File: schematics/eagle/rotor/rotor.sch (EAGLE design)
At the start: 55 parts, among them IC1 TXS0108, IC2 7815TV, J1 PL9823, J10 TB004-508-02BE, J2 pwr2, J3 Power, J4 Antenna, J5 Power, J6 CCW, J7 Brake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

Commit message: fix rotor input resistor
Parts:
- J10: value TB004-508-02BE -> 500Ω ├
- J9: value Rotor-Pwr-LED -> P.LED
- TEST-SW: value DPDT-SWITCH -> Test-Switch
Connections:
- removed net N$13: R3.1, TEST-SW.C-1, TEST-SW.C-2
- new net INPUT: R2.1, R3.1, TEST-SW.C-1, TEST-SW.C-2
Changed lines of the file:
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@@
 <layer number="18" name="Vias" color="2" fill="1" visible="no" active="no"/>
 <layer number="19" name="Unrouted" color="6" fill="1" visible="no" active="no"/>
-<layer number="20" name="Dimension" color="15" fill="1" visible="no" active="no"/>
+<layer number="20" name="Dimension" color="24" fill="1" visible="no" active="no"/>
 <layer number="21" name="tPlace" color="7" fill="1" visible="no" active="no"/>
 <layer number="22" name="bPlace" color="7" fill="1" visible="no" active="no"/>
-<layer number="23" name="tOrigins" color="15" fill="1" visible="no" active="no"/>
-<layer number="24" name="bOrigins" color="15" fill="1" visible="no" active="no"/>
+<layer number="23" name="tOrigins" color="13" fill="1" visible="no" active="no"/>
+<layer number="24" name="bOrigins" color="13" fill="1" visible="no" active="no"/>
 <layer number="25" name="tNames" color="7" fill="1" visible="no" active="no"/>
 <layer number="26" name="bNames" color="7" fill="1" visible="no" active="no"/>
@@
 <part name="C8" library="test" deviceset="C-US" device="C0805" package3d_urn="urn:adsk.eagle:package:6240337/1" value="104"/>
 <part name="C9" library="test" deviceset="C-US" device="C0805" package3d_urn="urn:adsk.eagle:package:6240337/1" value="104"/>
-<part name="J9" library="TB004-508-02BE" deviceset="TB004-508-02BE" device="" value="Rotor-Pwr-LED"/>
+<part name="J9" library="TB004-508-02BE" deviceset="TB004-508-02BE" device="" value="P.LED"/>
 <part name="SUPPLY5" library="Power_Symbols" library_urn="urn:adsk.eagle:library:16502351" deviceset="EGND" device="" value="GND"/>
 <part name="R20" library="test" deviceset="R-US_" device="M0805" package3d_urn="urn:adsk.eagle:package:6240587/1" value="1k"/>
@@
 <part name="J4" library="TB004-508-03BE" deviceset="TB004-508-03BE" device="" value="Antenna"/>
 <part name="SUPPLY4" library="Power_Symbols" library_urn="urn:adsk.eagle:library:16502351" deviceset="EGND" device="" value="GND"/>
-<part name="TEST-SW" library="ladyada" deviceset="DPDT-SWITCH" device=""/>
-<part name="J10" library="TB004-508-02BE" deviceset="TB004-508-02BE" device=""/>
+<part name="TEST-SW" library="ladyada" deviceset="DPDT-SWITCH" device="" value="Test-Switch"/>
+<part name="J10" library="TB004-508-02BE" deviceset="TB004-508-02BE" device="" value="500Ω ├"/>
 <part name="SUPPLY6" library="Power_Symbols" library_urn="urn:adsk.eagle:library:16502351" deviceset="EGND" device="" value="GND"/>
 </parts>
@@
 <wire x1="-220.98" y1="116.84" x2="-220.98" y2="104.14" width="0.1524" layer="91"/>
 <label x="-45.72" y="96.52" size="1.778" layer="95"/>
-<label x="-180.34" y="96.52" size="1.778" layer="95"/>
 <pinref part="J4" gate="G$1" pin="1"/>
 <label x="-220.98" y="106.68" size="1.778" layer="95" rot="R90"/>
@@
 </segment>
 </net>
-<net name="N$13" class="0">
+<net name="INPUT" class="0">
 <segment>
 <pinref part="TEST-SW" gate="G$1" pin="C-1"/>
@@
 <wire x1="-284.48" y1="104.14" x2="-279.4" y2="104.14" width="0.1524" layer="91"/>
 <wire x1="-284.48" y1="104.14" x2="-284.48" y2="96.52" width="0.1524" layer="91"/>
-<wire x1="-284.48" y1="96.52" x2="-17.78" y2="96.52" width="0.1524" layer="91"/>
 <junction x="-284.48" y="104.14"/>
 <pinref part="R3" gate="G$1" pin="1"/>
+<wire x1="-284.48" y1="96.52" x2="-157.48" y2="96.52" width="0.1524" layer="91"/>
+<wire x1="-157.48" y1="96.52" x2="-17.78" y2="96.52" width="0.1524" layer="91"/>
 <wire x1="-17.78" y1="96.52" x2="-17.78" y2="124.46" width="0.1524" layer="91"/>
-</segment>
-</net>
+<pinref part="R2" gate="G$1" pin="1"/>
+<wire x1="-157.48" y1="111.76" x2="-157.48" y2="96.52" width="0.1524" layer="91"/>
+<junction x="-157.48" y="96.52"/>
+<label x="-193.04" y="96.52" size="1.778" layer="95"/>
+</segment>
+</net>

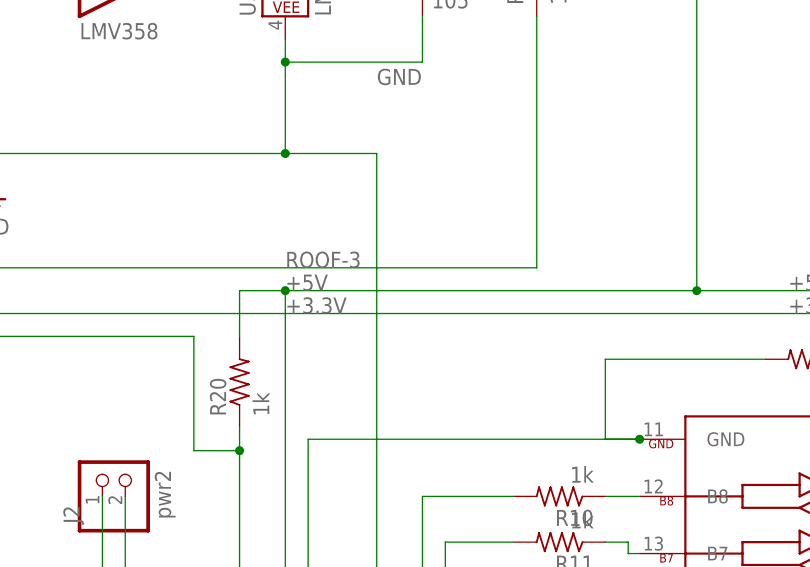
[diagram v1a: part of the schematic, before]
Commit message: v1.02 - fix transistors
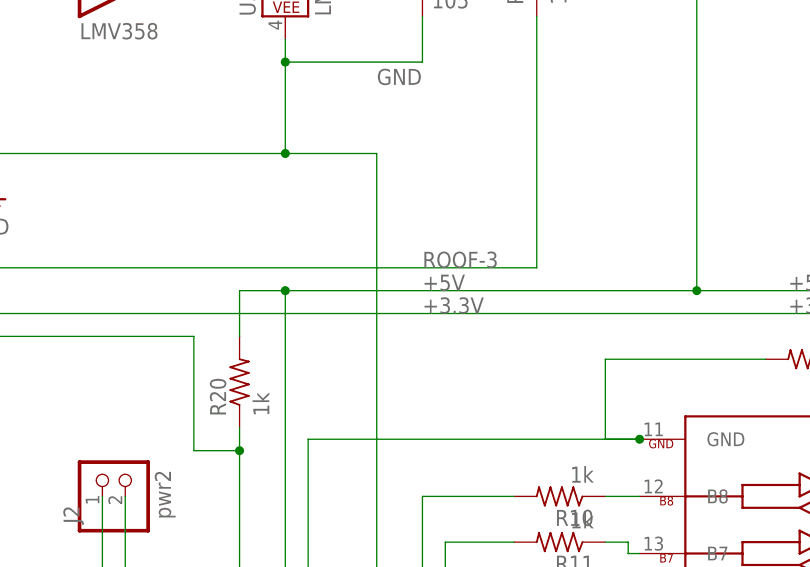
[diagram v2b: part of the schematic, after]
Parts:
- Q1: device test:2N2907CBE -> ladyada:2N2907EBC
- T1: device test:2N2222CBE -> ladyada:2N2222EBC
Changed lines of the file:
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@@
 <part name="J8" library="TB004-508-02BE" deviceset="TB004-508-02BE" device="" value="CW"/>
 <part name="R18" library="test" deviceset="R-US_" device="M0805" package3d_urn="urn:adsk.eagle:package:6240587/1" value="1k"/>
-<part name="Q1" library="test" deviceset="2N2907*" device="CBE" value="2N2907"/>
+<part name="Q1" library="ladyada" deviceset="2N2907*" device="EBC" package3d_urn="urn:adsk.eagle:package:6240647/1" value="2N2907"/>
 <part name="R19" library="test" deviceset="R-US_" device="M0805" package3d_urn="urn:adsk.eagle:package:6240587/1" value="1k"/>
 <part name="C8" library="test" deviceset="C-US" device="C0805" package3d_urn="urn:adsk.eagle:package:6240337/1" value="104"/>
@@
 <part name="SUPPLY5" library="Power_Symbols" library_urn="urn:adsk.eagle:library:16502351" deviceset="EGND" device="" value="GND"/>
 <part name="R20" library="test" deviceset="R-US_" device="M0805" package3d_urn="urn:adsk.eagle:package:6240587/1" value="1k"/>
-<part name="T1" library="test" deviceset="2N2222" device="CBE" value="2N2222"/>
+<part name="T1" library="ladyada" deviceset="2N2222" device="EBC" package3d_urn="urn:adsk.eagle:package:6240647/1" value="2N2222"/>
 <part name="D2" library="test" deviceset="DIODE" device="SMA" package3d_urn="urn:adsk.eagle:package:6240747/1" value="FR107"/>
 <part name="C10" library="test" deviceset="C-US" device="C0805" package3d_urn="urn:adsk.eagle:package:6240337/1" value="106"/>
@@
 <wire x1="-10.16" y1="17.78" x2="-10.16" y2="20.32" width="0.1524" layer="91"/>
 <junction x="-10.16" y="20.32"/>
-<label x="-45.72" y="93.98" size="1.778" layer="95"/>
+<label x="-30.48" y="93.98" size="1.778" layer="95"/>
 <wire x1="-45.72" y1="93.98" x2="-50.8" y2="93.98" width="0.1524" layer="91"/>
 <junction x="-45.72" y="93.98"/>
@@
 <wire x1="33.02" y1="17.78" x2="33.02" y2="20.32" width="0.1524" layer="91"/>
 <junction x="33.02" y="20.32"/>
-<label x="-45.72" y="91.44" size="1.778" layer="95"/>
+<label x="-30.48" y="91.44" size="1.778" layer="95"/>
 </segment>
 </net>
@@
 <segment>
 <wire x1="-220.98" y1="116.84" x2="-220.98" y2="104.14" width="0.1524" layer="91"/>
-<label x="-45.72" y="96.52" size="1.778" layer="95"/>
+<label x="-30.48" y="96.52" size="1.778" layer="95"/>
 <pinref part="J4" gate="G$1" pin="1"/>
 <label x="-220.98" y="106.68" size="1.778" layer="95" rot="R90"/>

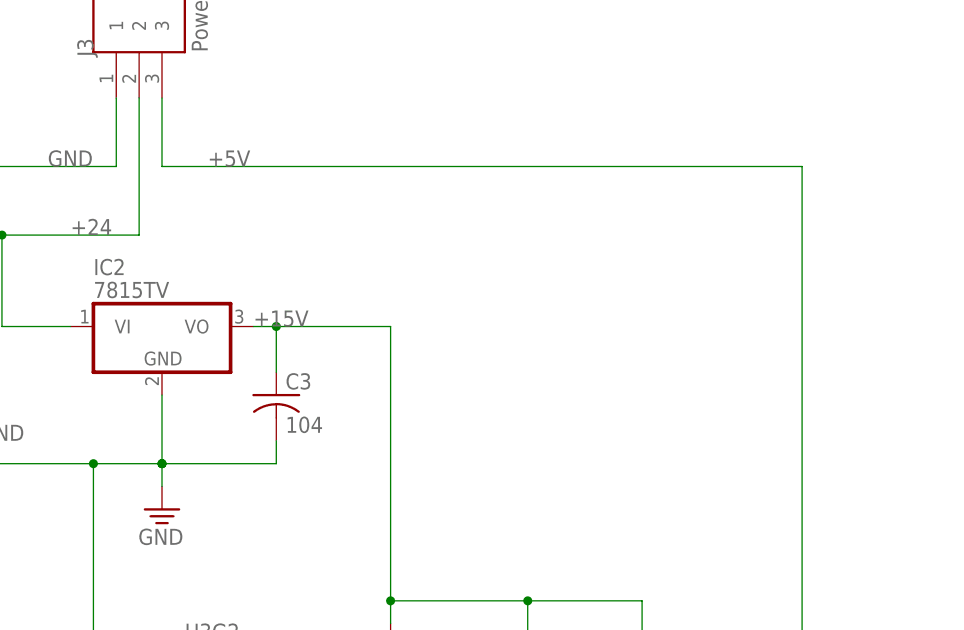
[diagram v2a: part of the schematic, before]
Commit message: 2n2222 diagram
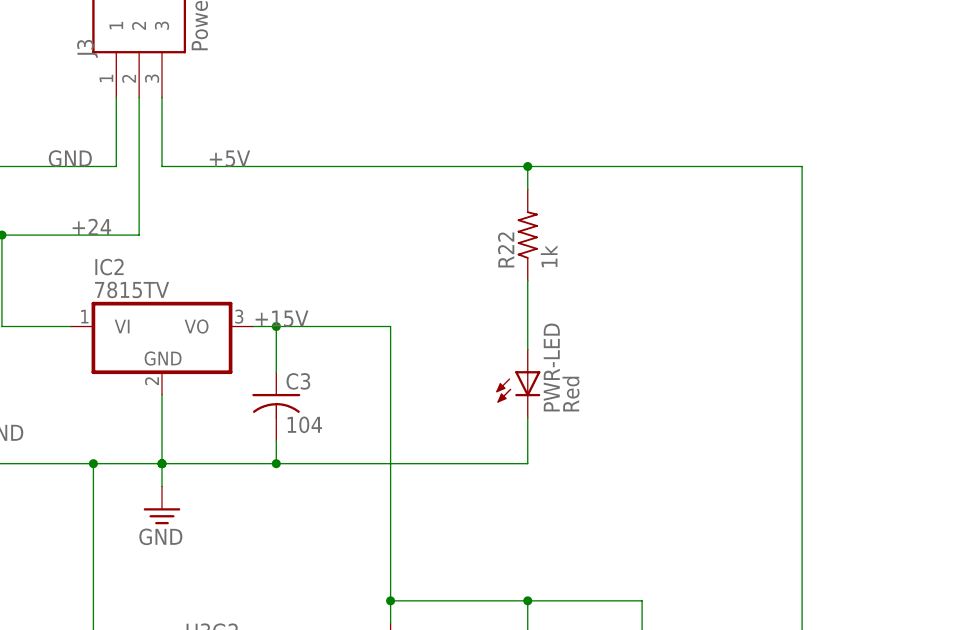
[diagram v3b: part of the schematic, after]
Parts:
- added PWR-LED: Red, ladyada:LEDCHIP-LED0805
- added R22: 1k, test:R-US_M0805
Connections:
- new net N$13: PWR-LED.A, R22.1
- net +5V: now also R22.2
- net GND: now also PWR-LED.C
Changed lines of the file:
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@@
 <part name="J10" library="TB004-508-02BE" deviceset="TB004-508-02BE" device="" value="500Ω ├"/>
 <part name="SUPPLY6" library="Power_Symbols" library_urn="urn:adsk.eagle:library:16502351" deviceset="EGND" device="" value="GND"/>
+<part name="R22" library="test" deviceset="R-US_" device="M0805" package3d_urn="urn:adsk.eagle:package:6240587/1" value="1k"/>
+<part name="PWR-LED" library="ladyada" deviceset="LED" device="CHIP-LED0805" package3d_urn="urn:adsk.eagle:package:6240557/1" value="Red"/>
 </parts>
 <sheets>
@@
 <instance part="SUPPLY6" gate="G$1" x="-304.8" y="53.34" smashed="yes">
 <attribute name="VALUE" x="-304.927" y="49.403" size="1.778" layer="96" align="bottom-center"/>
+</instance>
+<instance part="R22" gate="G$1" x="-30.48" y="180.34" smashed="yes" rot="R90">
+<attribute name="NAME" x="-31.9786" y="176.53" size="1.778" layer="95" rot="R90"/>
+<attribute name="VALUE" x="-27.178" y="176.53" size="1.778" layer="96" rot="R90"/>
+</instance>
+<instance part="PWR-LED" gate="G$1" x="-30.48" y="165.1" smashed="yes">
+<attribute name="NAME" x="-26.924" y="160.528" size="1.778" layer="95" rot="R90"/>
+<attribute name="VALUE" x="-24.765" y="160.528" size="1.778" layer="96" rot="R90"/>
 </instance>
 </instances>
@@
 <pinref part="J3" gate="G$1" pin="3"/>
 <wire x1="-71.12" y1="195.58" x2="-71.12" y2="187.96" width="0.1524" layer="91"/>
-<wire x1="-71.12" y1="187.96" x2="0" y2="187.96" width="0.1524" layer="91"/>
+<wire x1="-71.12" y1="187.96" x2="-30.48" y2="187.96" width="0.1524" layer="91"/>
+<wire x1="-30.48" y1="187.96" x2="0" y2="187.96" width="0.1524" layer="91"/>
 <wire x1="0" y1="187.96" x2="0" y2="93.98" width="0.1524" layer="91"/>
 <junction x="0" y="93.98"/>
@@
 <pinref part="Q1" gate="G$1" pin="C"/>
 <wire x1="27.94" y1="-66.04" x2="27.94" y2="-76.2" width="0.1524" layer="91"/>
+<pinref part="R22" gate="G$1" pin="2"/>
+<wire x1="-30.48" y1="185.42" x2="-30.48" y2="187.96" width="0.1524" layer="91"/>
+<junction x="-30.48" y="187.96"/>
 </segment>
 </net>
@@
 <junction x="-231.14" y="60.96"/>
 <junction x="-304.8" y="60.96"/>
+<pinref part="PWR-LED" gate="G$1" pin="C"/>
+<wire x1="-58.42" y1="154.94" x2="-30.48" y2="154.94" width="0.1524" layer="91"/>
+<wire x1="-30.48" y1="154.94" x2="-30.48" y2="160.02" width="0.1524" layer="91"/>
+<junction x="-58.42" y="154.94"/>
 </segment>
 </net>
@@
 </segment>
 </net>
+<net name="N$13" class="0">
+<segment>
+<pinref part="PWR-LED" gate="G$1" pin="A"/>
+<pinref part="R22" gate="G$1" pin="1"/>
+<wire x1="-30.48" y1="167.64" x2="-30.48" y2="175.26" width="0.1524" layer="91"/>
+</segment>
+</net>
